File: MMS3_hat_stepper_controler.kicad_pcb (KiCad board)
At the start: 4 copper layers, 90 x 50 mm, 5 parts, among them J1 86093488324755V1LF, J4 Conn_01x16_Socket

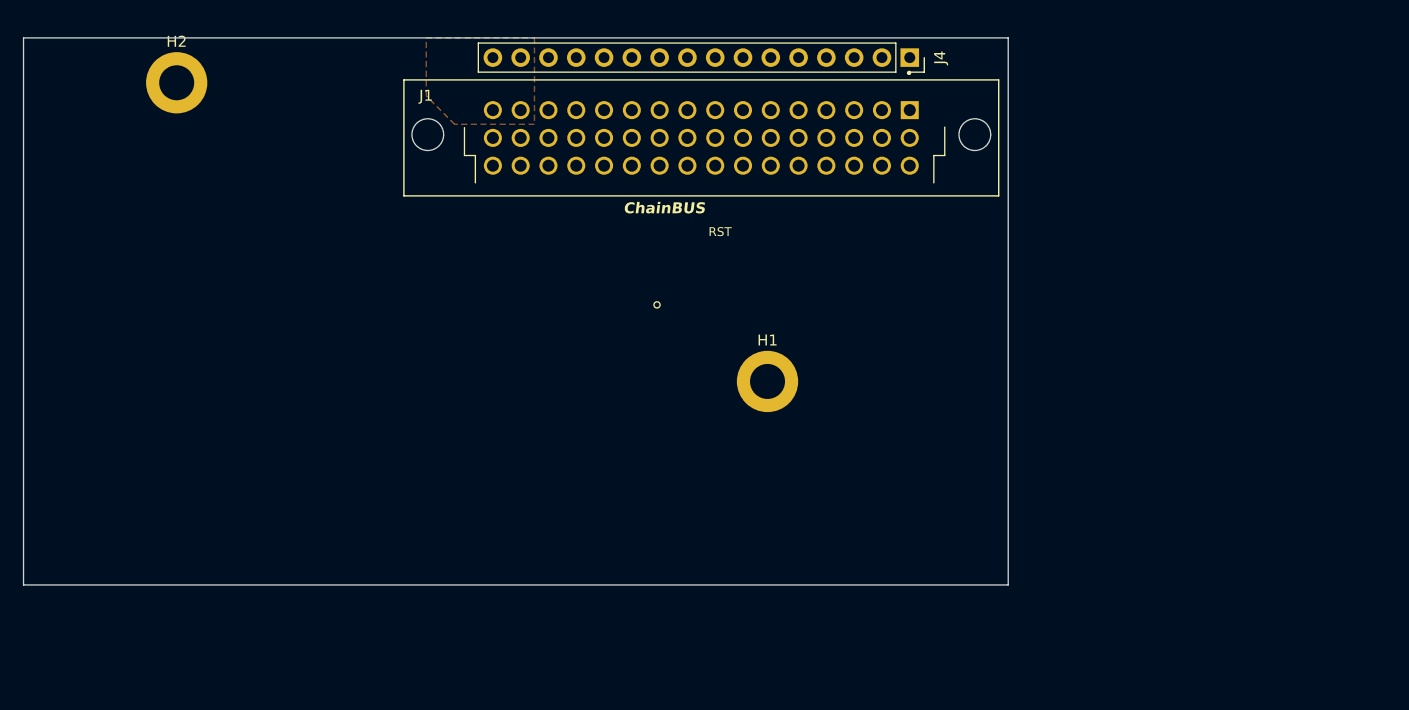
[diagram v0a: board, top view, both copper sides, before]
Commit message: initial component placement
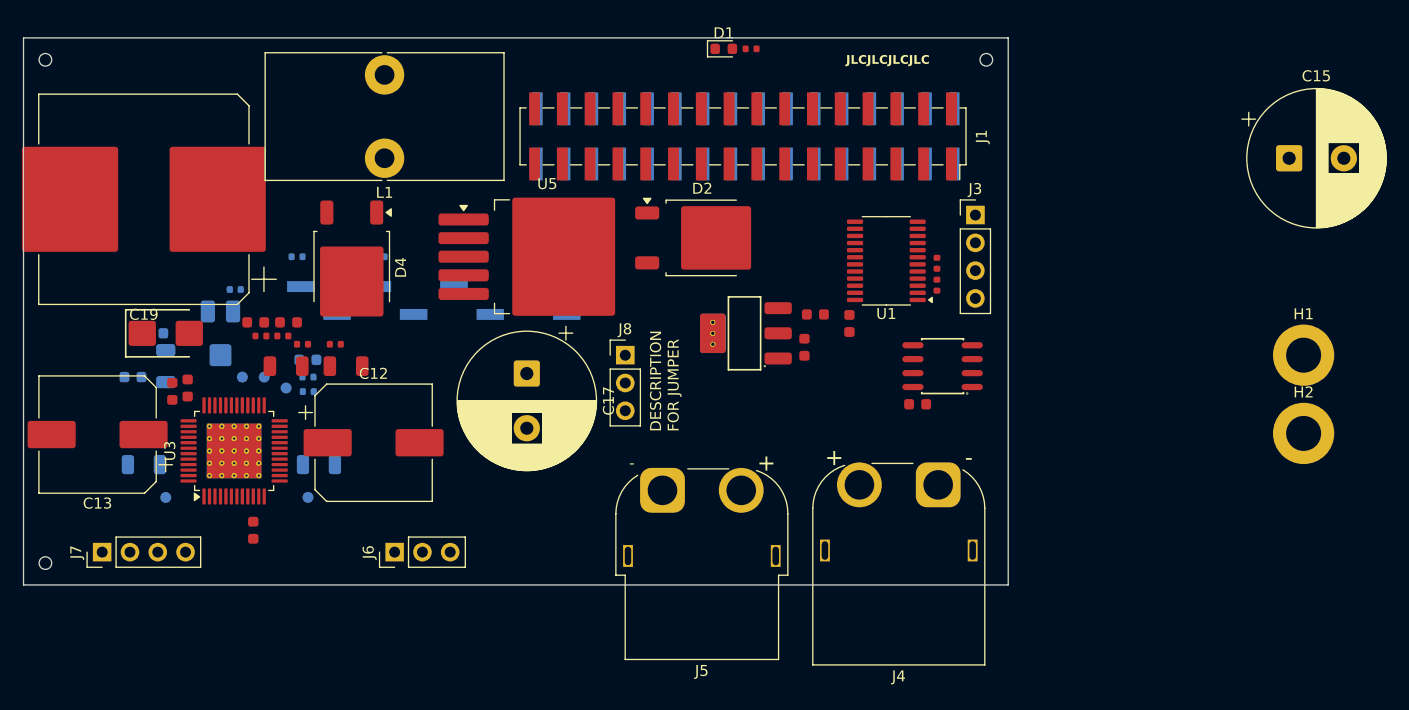
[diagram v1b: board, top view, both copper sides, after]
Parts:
- removed G***: LOGO, QRcode:QR
- added C1: 100nF, PCM_JLCPCB:C_0603, F.Cu at (155.5, 114.1)
- added C10: 4.7uF, PCM_JLCPCB:C_1206, F.Cu at (104.0, 118.0)
- added C11: 4.7uF, PCM_JLCPCB:C_1206, F.Cu at (109.5, 118.0)
- added C12: 100u, Capacitor_SMD:CP_Elec_10x12.5, F.Cu at (112.0, 125.0)
- added C13: 100u, Capacitor_SMD:CP_Elec_10x12.5, F.Cu at (86.8, 124.3)
- added C14: 10uF, PCM_JLCPCB:C_0603, F.Cu at (152.4, 113.3)
- added C15: 330u, Capacitor_THT:CP_Radial_D12.5mm_P5.00mm, F.Cu at (195.7, 99.0)
- added C16: 10uF, PCM_JLCPCB:C_0603, F.Cu at (151.4, 116.3)
- added C17: 330u, Capacitor_THT:CP_Radial_D12.5mm_P5.00mm, F.Cu at (126.0, 118.7)
- added C18: 3.3nF, PCM_JLCPCB:C_0603, B.Cu at (106.0, 117.4)
- added C19: 330u, Capacitor_SMD:CP_Elec_18x17.5, F.Cu at (91.0, 102.8)
- added C2: 100nF, PCM_JLCPCB:C_0603, F.Cu at (161.7, 121.5)
- added C3: 100nF, PCM_JLCPCB:C_0603, F.Cu at (101.0, 133.0)
- added C4: 4.7uF, PCM_JLCPCB:C_0603, B.Cu at (92.0, 115.0)
- added C5: 22nF, PCM_JLCPCB:C_0603, F.Cu at (95.0, 120.0)
- added C6: 470nF, PCM_JLCPCB:C_0603, B.Cu at (90.0, 119.0)
- added C7: 100nF, PCM_JLCPCB:C_0603, F.Cu at (93.6, 120.3)
- added C8: 100nF, PCM_JLCPCB:C_0603, F.Cu at (101.2, 114.0)
- added C9: 100nF, PCM_JLCPCB:C_0603, F.Cu at (104.2, 114.0)
- added D1: LED, LED_SMD:LED_0603_1608Metric, F.Cu at (144.0, 89.0)
- added D2: MBRD10100CTTR, Package_TO_SOT_SMD:TO-252-2, F.Cu at (142.0, 106.3)
- added D3: SMBJ43CA, PCM_JLCPCB:D_SMB, F.Cu at (93.0, 115.0)
- added D4: MBRD10100CTTR, Package_TO_SOT_SMD:TO-252-2, F.Cu at (110.0, 109.0)
- added H3: ~, PCM_JLCPCB:Hole_Tooling_JLCPCB, F.Cu at (168.0, 90.0)
- added H4: ~, PCM_JLCPCB:Hole_Tooling_JLCPCB, F.Cu at (82.0, 90.0)
- added H5: ~, PCM_JLCPCB:Hole_Tooling_JLCPCB, F.Cu at (82.0, 136.0)
- added J10: Conn_01x02, Connector_PinHeader_2.54mm:PinHeader_1x02_P2.54mm_Vertical_SMD_Pin1Right, B.Cu at (121.0, 112.0)
- added J11: ~, Connector_PinHeader_2.54mm:PinHeader_1x02_P2.54mm_Vertical_SMD_Pin1Right, B.Cu at (114.0, 112.0)
- added J12: Conn_01x02, Connector_PinHeader_2.54mm:PinHeader_1x02_P2.54mm_Vertical_SMD_Pin1Right, B.Cu at (107.0, 112.0)
- added J2: Chainbus Out, Connector_PinSocket_2.54mm:PinSocket_2x16_P2.54mm_Vertical_SMD, B.Cu at (146.0, 97.0)
- added J3: Conn_01x04_Pin, Connector_PinHeader_2.54mm:PinHeader_1x04_P2.54mm_Vertical, F.Cu at (167.0, 104.2)
- added J5: AMASS XT60 Female, XT60:AMASS_XT60PW-F_1x02_P7.20mm_Horizontal, F.Cu at (138.4, 129.3)
- added J6: Encoder connector, Connector_PinHeader_2.54mm:PinHeader_1x03_P2.54mm_Vertical, F.Cu at (113.9, 135.0)
- added J7: Motor connector, Connector_PinHeader_2.54mm:PinHeader_1x04_P2.54mm_Vertical, F.Cu at (87.2, 135.0)
- added J8: Conn_01x03_Pin, Connector_PinHeader_2.54mm:PinHeader_1x03_P2.54mm_Vertical, F.Cu at (135.0, 117.0)
- added J9: Conn_01x02, Connector_PinHeader_2.54mm:PinHeader_1x02_P2.54mm_Vertical_SMD_Pin1Right, B.Cu at (128.0, 112.0)
- added L1: 100uH 5A, Inductor_THT:L_Toroid_Vertical_L21.6mm_W11.4mm_P7.62mm_Pulse_KM-3, F.Cu at (113.0, 99.0)
- added PN1: ~, PCM_JLCPCB:Part_Num_JLCPCB, F.Cu at (159.0, 90.0)
- added R1: 330Ω, PCM_JLCPCB:R_0402, F.Cu at (146.5, 89.0)
- added R10: 33kΩ, PCM_JLCPCB:R_0402, F.Cu at (105.5, 116.0)
- added R11: 33kΩ, PCM_JLCPCB:R_0402, F.Cu at (108.5, 116.0)
- added R12: 1kΩ, PCM_JLCPCB:R_0402, B.Cu at (106.0, 120.3)
- added R13: 18.7k, PCM_JLCPCB:R_0402, B.Cu at (106.0, 119.0)
- added R14: 16.5k, PCM_JLCPCB:R_0402, B.Cu at (119.5, 108.0)
- added R15: 9.53k, PCM_JLCPCB:R_0402, B.Cu at (112.5, 108.0)
- added R16: 5.11k, PCM_JLCPCB:R_0402, B.Cu at (105.0, 108.0)
- added R2: 10kΩ, PCM_JLCPCB:R_0402, F.Cu at (163.5, 108.6)
- added R3: 10kΩ, PCM_JLCPCB:R_0402, F.Cu at (163.5, 110.6)
- added R4: 0603/3R3, PCM_JLCPCB:R_1206, B.Cu at (93.0, 118.0)
- added R5: 100kΩ, PCM_JLCPCB:R_0402, B.Cu at (99.3, 111.0)
- added R6: 1206, 0R15, 0.5W, PCM_JLCPCB:R_1206, B.Cu at (91.0, 127.0)
- added R7: 1206, 0R15, 0.5W, PCM_JLCPCB:R_1206, B.Cu at (107.0, 127.0)
- added R8: 33kΩ, PCM_JLCPCB:R_0402, F.Cu at (101.7, 115.2)
- added R9: 33kΩ, PCM_JLCPCB:R_0402, F.Cu at (103.7, 115.2)
- added RV1: 100K TRIM, Potentiometer_SMD:Potentiometer_Vishay_TS53YJ_Vertical, B.Cu at (98.0, 115.0)
- added TP1: TestPoint, TestPoint:TestPoint_Pad_D1.0mm, B.Cu at (100.0, 119.0)
- added TP2: TestPoint, TestPoint:TestPoint_Pad_D1.0mm, B.Cu at (102.0, 119.0)
- added TP3: TestPoint, TestPoint:TestPoint_Pad_D1.0mm, B.Cu at (104.0, 120.0)
- added TP4: TestPoint, TestPoint:TestPoint_Pad_D1.0mm, B.Cu at (93.0, 130.0)
- added TP5: TestPoint, TestPoint:TestPoint_Pad_D1.0mm, B.Cu at (106.0, 130.0)
- added U1: SN74CB3Q3384APW, Package_SO:TSSOP-24_4.4x7.8mm_P0.65mm, F.Cu at (158.9, 108.4)
- added U2: M24C64, PCM_JLCPCB:SOIC-8_L5.0-W4.0-P1.27-LS6.0-BL, F.Cu at (164.0, 118.0)
- added U3: TMC5130A-TA, Package_QFP:TQFP-48-1EP_7x7mm_P0.5mm_EP5x5mm_ThermalVias, F.Cu at (99.2, 125.8)
- added U4: AMS1117, PCM_JLCPCB:SOT-223-3_L6.5-W3.4-P2.30-LS7.0-BR, F.Cu at (146.0, 115.0)
- added U5: LM2596HVS-ADJRG, Package_TO_SOT_SMD:TO-263-5_TabPin3, F.Cu at (127.9, 108.0)
- J1: value 86093488324755V1LF -> Chainbus In; footprint Library:AMPHENOL_86093488324755V1LF -> Connector_PinSocket_2.54mm:PinSocket_2x16_P2.54mm_Vertical_SMD
- J4: value Conn_01x16_Socket -> AMASS XT60 Male; footprint Connector_PinSocket_2.54mm:PinSocket_1x16_P2.54mm_Vertical -> XT60:AMASS_XT60PW-M_1x02_P7.20mm_Horizontal
- moved H2 107.9 mm to (197.0, 124.2)
- moved H1 49.1 mm to (197.0, 117.0)
- moved J4 39.1 mm to (163.6, 128.8), turned to 180 degrees
- moved J1 3.81 mm to (145.8, 97.0), turned to -90 degrees
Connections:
- J4 pad 1: unconnected-(J4-Pin_1-Pad1) -> GND
- J4 pad 2: unconnected-(J4-Pin_2-Pad2) -> Vin
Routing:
- removed copper zone on In2.Cu, net +3V3
- removed copper zone on F.Cu, net +5V
- removed copper zone on In2.Cu, net BRD_VIN
- removed copper zone on In1.Cu, net GND
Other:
- board text added: "DESCRIPTION FOR JUMPER"
- board text removed: "2"
- board text removed: "3V3"
- board text removed: "5V0"
- board text removed: "ChainBUS"
- board text removed: "ChainBus"
- board text removed: "DEVICE ESD SENSETIVE"
- board text removed: "DIN41612"
- board text removed: "Encloshure is supposed to have 2mm walls :)"
- board text removed: "Ethernet Port"
- board text removed: "FW VER. MC1"
- board text removed: "FW VER. MC2"
- board text removed: "G"
- board text removed: "GND"
- board text removed: "IEC 60664-1 Material Group III (CTI < 400; typical FR-4 = IIIa): 1.25 mm"
- board text removed: "IO R G"
- board text removed: "MMS"
- board text removed: "N/C"
- board text removed: "Power Connector"
- board text removed: "QC"
- board text removed: "RST"
- board text removed: "SN"
- board text removed: "This is prototype device It is not certified according to current EU laws. Do not sell or use outside of research purposes."
- board text removed: "VIN"
- board text removed: "Ymin LKME5001J102MF"
- board text removed: "arthorh.github.io/ChainBus"
- board text removed: "connector powered by"
- board text removed: "i"

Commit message: revision
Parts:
- removed D2: MBRD10100CTTR, Package_TO_SOT_SMD:TO-252-2
- added C20: 3.3nF, PCM_JLCPCB:C_0603, F.Cu at (213.7, 66.7)
- added C21: 100nF, PCM_JLCPCB:C_0603, F.Cu at (213.7, 68.9)
- added C22: 100nF, PCM_JLCPCB:C_0603, F.Cu at (213.7, 71.2)
- added D5: MBRD10100CTTR, SMC_MBRD10100CTTR:TO-252-3_L6.5-W5.8-P4.58-TL, F.Cu at (233.5, 79.0)
- added H6: ~, PCM_JLCPCB:Hole_Tooling_JLCPCB, F.Cu at (256.7, 155.6)
- added H7: ~, PCM_JLCPCB:Hole_Tooling_JLCPCB, F.Cu at (256.7, 158.6)
- added R17: 33kΩ, PCM_JLCPCB:R_0402, F.Cu at (210.4, 62.0)
- added R18: 33kΩ, PCM_JLCPCB:R_0402, F.Cu at (210.4, 63.8)
- added TP6: TestPoint, TestPoint:TestPoint_Pad_D1.0mm, F.Cu at (208.6, 112.4)
- C14: value 10uF -> 100u; footprint PCM_JLCPCB:C_0603 -> Capacitor_SMD:CP_Elec_10x12.5
- C15: value 330u -> 100u; footprint Capacitor_THT:CP_Radial_D12.5mm_P5.00mm -> Capacitor_SMD:CP_Elec_10x12.5
- C17: value 330u -> 10uF; footprint Capacitor_THT:CP_Radial_D12.5mm_P5.00mm -> PCM_JLCPCB:C_0603
- C18: value 3.3nF -> 100nF; moved to F.Cu
- C19: value 330u -> 100nF; footprint Capacitor_SMD:CP_Elec_18x17.5 -> PCM_JLCPCB:C_0603
- C4, C6, R12, R13, R14, R15, R16, R4, R5, R6, R7, TP1, TP2, TP3, TP4, TP5: moved to F.Cu
- D4: footprint Package_TO_SOT_SMD:TO-252-2 -> SMC_MBRD10100CTTR:TO-252-3_L6.5-W5.8-P4.58-TL
- H1: footprint MountingHole:MountingHole_3.2mm_M3_DIN965_Pad -> MountingHole:MountingHole_2.7mm_M2.5_DIN965_Pad_TopOnly
- H2: footprint MountingHole:MountingHole_3.2mm_M3_DIN965_Pad -> MountingHole:MountingHole_2.7mm_M2.5_DIN965
- H3, H4: value ~ -> M3 mount; footprint PCM_JLCPCB:Hole_Tooling_JLCPCB -> MountingHole:MountingHole_2.7mm_M2.5_DIN965
- J1: value Chainbus In -> Chainbus in
- J10, J12, J9: footprint Connector_PinHeader_2.54mm:PinHeader_1x02_P2.54mm_Vertical_SMD_Pin1Right -> Connector_PinHeader_2.54mm:PinHeader_1x02_P2.54mm_Vertical; moved to F.Cu
- J11: value ~ -> Conn_01x02; footprint Connector_PinHeader_2.54mm:PinHeader_1x02_P2.54mm_Vertical_SMD_Pin1Right -> Connector_PinHeader_2.54mm:PinHeader_1x02_P2.54mm_Vertical; moved to F.Cu
- J6: footprint Connector_PinHeader_2.54mm:PinHeader_1x03_P2.54mm_Vertical -> Connector_JST:JST_XH_S3B-XH-A-1_1x03_P2.50mm_Horizontal
- J7: footprint Connector_PinHeader_2.54mm:PinHeader_1x04_P2.54mm_Vertical -> Connector_JST:JST_XH_S4B-XH-A_1x04_P2.50mm_Horizontal
- RV1: footprint Potentiometer_SMD:Potentiometer_Vishay_TS53YJ_Vertical -> Potentiometer_THT:Potentiometer_Bourns_3386W_Horizontal; moved to F.Cu
- moved H5 175.5 mm to (256.7, 152.6)
- moved L1 129.6 mm to (240.0, 73.0)
- moved D3 127.9 mm to (220.3, 102.8)
- moved U5 127.1 mm to (252.2, 81.5)
- moved J8 126.9 mm to (254.0, 73.0), turned to 180 degrees
- moved D4 126.5 mm to (236.5, 110.0), turned to 0 degrees
- moved C19 125.7 mm to (213.7, 75.7), turned to 0 degrees
- moved D1 121.7 mm to (260.7, 123.5)
- moved R9 118.6 mm to (222.2, 116.8)
- moved C9 118.5 mm to (222.8, 115.5)
- moved R8 117.8 mm to (219.5, 116.8)
- moved C8 117.8 mm to (219.0, 115.5)
- moved R12 117.8 mm to (210.4, 65.7)
- moved C4 116.9 mm to (208.5, 124.0), turned to 90 degrees
- moved C6 116.4 mm to (206.3, 124.0), turned to 90 degrees
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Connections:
- C14 pad 1: +5V -> U_reg
- C15 pad 1: Net-(J8-Pin_1) -> U_reg
- C16 pad 1: 3V3 -> +5V
- C17 pad 1: Net-(J8-Pin_1) -> +3V3
- C18 pad 1: Net-(J10-Pin_1) -> Net-(J8-Pin_1)
- C18 pad 2: U_reg -> Net-(C18-Pad2)
- C19 pad 1: U_reg -> Net-(C18-Pad2)
- C3 pad 1: 3V3 -> +3V3
- C8 pad 2: Net-(C8-Pad2) -> Net-(C10-Pad2)
- C9 pad 1: Net-(C8-Pad2) -> Net-(C10-Pad2)
- D4 pad 1: Net-(D4-K) -> Vin
- D4 pad 2: GND -> BRD_VIN
- D4 pad 3: (no net) -> Vin
- J1 pad 1: /Bus_switch/Chainbus_In.RX -> GND
- J1 pad 10: /Interboard_connector/SEL7 -> /Interboard_connector/SEL5
- J1 pad 11: /Interboard_connector/SEL6 -> BRD_VIN
- J1 pad 12: /Interboard_connector/SEL5 -> /Interboard_connector/SEL6
- J1 pad 13: /Interboard_connector/SEL4 -> BRD_VIN
- J1 pad 14: /Interboard_connector/SEL3 -> /Interboard_connector/SEL7
- J1 pad 15: /Interboard_connector/SEL2 -> BRD_VIN
- J1 pad 16: /Bus_switch/SEL1 -> /Interboard_connector/SEL8
- J1 pad 18: +5V -> /Bus_switch/Chainbus_In.SDA
- J1 pad 19: +5V -> GND
- J1 pad 2: /Bus_switch/Chainbus_In.TX -> /Bus_switch/SEL1
- J1 pad 20: GND -> /Bus_switch/Chainbus_In.SCL
- J1 pad 21: BRD_VIN -> GND
- J1 pad 22: BRD_VIN -> /Bus_switch/Chainbus_In.CS
- J1 pad 23: BRD_VIN -> GND
- J1 pad 24: BRD_VIN -> /Bus_switch/Chainbus_In.SCK
- J1 pad 25: GND -> unconnected-(J1-Pin_25-Pad25)
- J1 pad 26: GND -> /Bus_switch/Chainbus_In.MOSI
- J1 pad 27: GND -> unconnected-(J1-Pin_27-Pad27)
- J1 pad 28: GND -> /Bus_switch/Chainbus_In.MISO
- J1 pad 29: unconnected-(J1-Pin_29-Pad29) -> +12V stby
- J1 pad 3: /Bus_switch/Chainbus_In.MISO -> +5V
- J1 pad 30: unconnected-(J1-Pin_30-Pad30) -> /Bus_switch/Chainbus_In.TX
- J1 pad 31: +12V stby -> GND
- J1 pad 32: GND -> /Bus_switch/Chainbus_In.RX
- J1 pad 4: /Bus_switch/Chainbus_In.MOSI -> /Interboard_connector/SEL2
- J1 pad 5: /Bus_switch/Chainbus_In.SCK -> +5V
- J1 pad 6: /Bus_switch/Chainbus_In.CS -> /Interboard_connector/SEL3
- J1 pad 7: /Bus_switch/Chainbus_In.SCL -> GND
- J1 pad 8: /Bus_switch/Chainbus_In.SDA -> /Interboard_connector/SEL4
- J1 pad 9: /Interboard_connector/SEL8 -> BRD_VIN
- J2 pad 1: /Bus_switch/Chainbus_In.RX -> /Interboard_connector/SEL2
- J2 pad 10: /Interboard_connector/SEL8 -> BRD_VIN
- J2 pad 12: /Interboard_connector/SEL6 -> BRD_VIN
- J2 pad 13: /Interboard_connector/SEL5 -> /Interboard_connector/SEL8
- J2 pad 14: /Interboard_connector/SEL4 -> BRD_VIN
- J2 pad 15: /Interboard_connector/SEL3 -> unconnected-(J2-Pin_15-Pad15)
- J2 pad 16: /Interboard_connector/SEL2 -> BRD_VIN
- J2 pad 17: GND -> /Bus_switch/Chainbus_In.SDA
- J2 pad 18: +5V -> GND
- J2 pad 19: +5V -> /Bus_switch/Chainbus_In.SCL
- J2 pad 2: /Bus_switch/Chainbus_In.TX -> GND
- J2 pad 21: BRD_VIN -> /Bus_switch/Chainbus_In.CS
- J2 pad 22: BRD_VIN -> GND
- J2 pad 23: BRD_VIN -> /Bus_switch/Chainbus_In.SCK
- J2 pad 24: BRD_VIN -> GND
- J2 pad 25: GND -> /Bus_switch/Chainbus_In.MOSI
- J2 pad 26: GND -> unconnected-(J2-Pin_26-Pad26)
- J2 pad 27: GND -> /Bus_switch/Chainbus_In.MISO
- J2 pad 28: GND -> unconnected-(J2-Pin_28-Pad28)
- J2 pad 29: unconnected-(J2-Pin_29-Pad29) -> /Bus_switch/Chainbus_In.TX
- J2 pad 3: /Bus_switch/Chainbus_In.MISO -> /Interboard_connector/SEL3
- J2 pad 30: unconnected-(J2-Pin_30-Pad30) -> +12V stby
- J2 pad 31: +12V stby -> /Bus_switch/Chainbus_In.RX
- J2 pad 4: /Bus_switch/Chainbus_In.MOSI -> +5V
- J2 pad 5: /Bus_switch/Chainbus_In.SCK -> /Interboard_connector/SEL4
- J2 pad 6: /Bus_switch/Chainbus_In.CS -> +5V
- J2 pad 7: /Bus_switch/Chainbus_In.SCL -> /Interboard_connector/SEL5
- J2 pad 8: /Bus_switch/Chainbus_In.SDA -> GND
- J2 pad 9: unconnected-(J2-Pin_9-Pad9) -> /Interboard_connector/SEL6
- L1 pad 1: Net-(D4-K) -> Net-(D5-K)
- R10 pad 1: U_reg -> Net-(J8-Pin_1)
- R10 pad 2: Net-(C10-Pad2) -> Net-(C18-Pad2)
- R11 pad 1: Net-(C10-Pad2) -> Net-(C18-Pad2)
- R8 pad 2: Net-(C8-Pad2) -> Net-(C10-Pad2)
- R9 pad 1: Net-(C8-Pad2) -> Net-(C10-Pad2)
- U2 pad 8: 3V3 -> +3V3
- U3 pad 10: 3V3 -> +3V3
- U4 pad 2: 3V3 -> +3V3
- U4 pad 4: 3V3 -> +3V3
- U5 pad 2: Net-(D4-K) -> Net-(D5-K)
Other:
- board text removed: "DESCRIPTION FOR JUMPER"
